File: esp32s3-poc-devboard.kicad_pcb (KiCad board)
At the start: 4 copper layers, 74 x 66.8 mm, 104 parts, among them J1 24VDC, J2 Conn_01x01_Pin, J3 USB_C_Receptacle_USB2.0_14P, J4 USB_C_Receptacle_USB2.0_14P, J5 Screw_Terminal_01x06, J6 Conn_Coaxial, J7 Conn_01x16_Pin, J8 Screw_Terminal_01x04, Q3 MMDT5551, SW1 SW_Push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

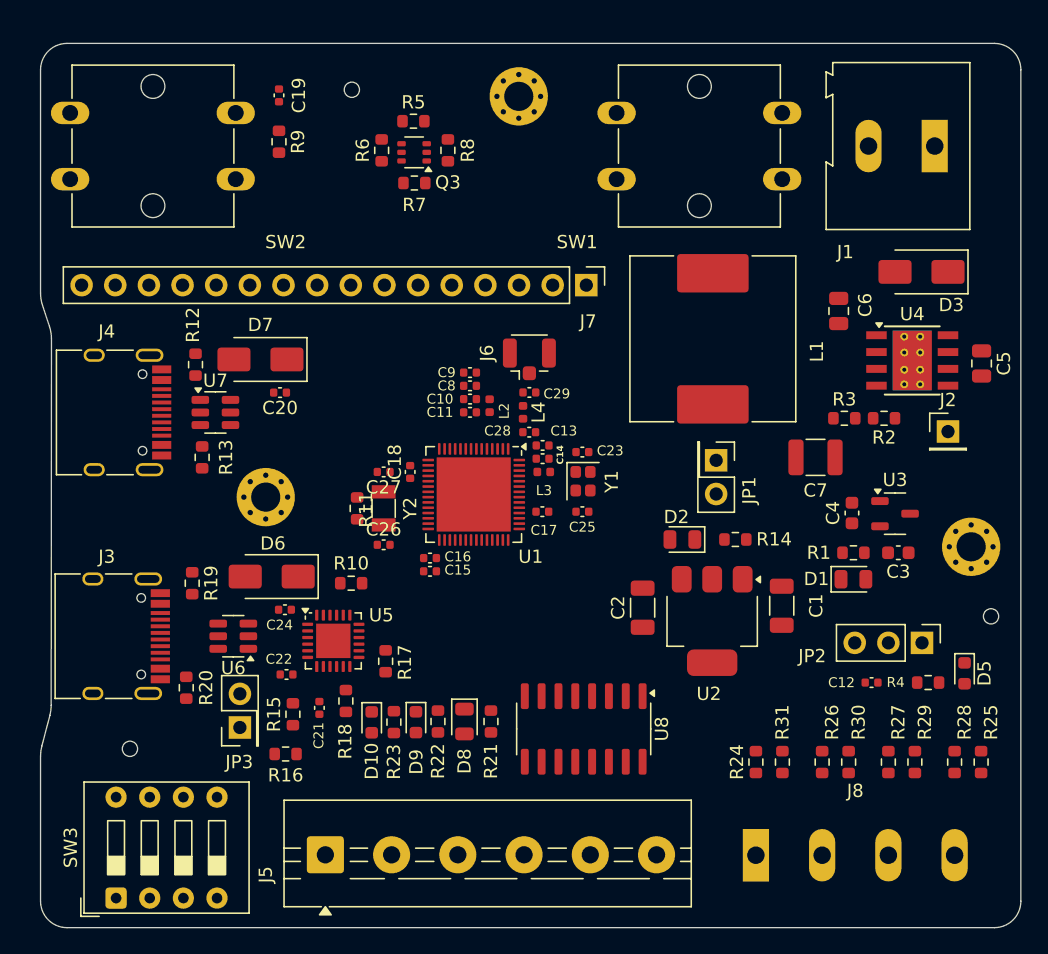
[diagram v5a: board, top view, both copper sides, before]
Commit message: add fiducials
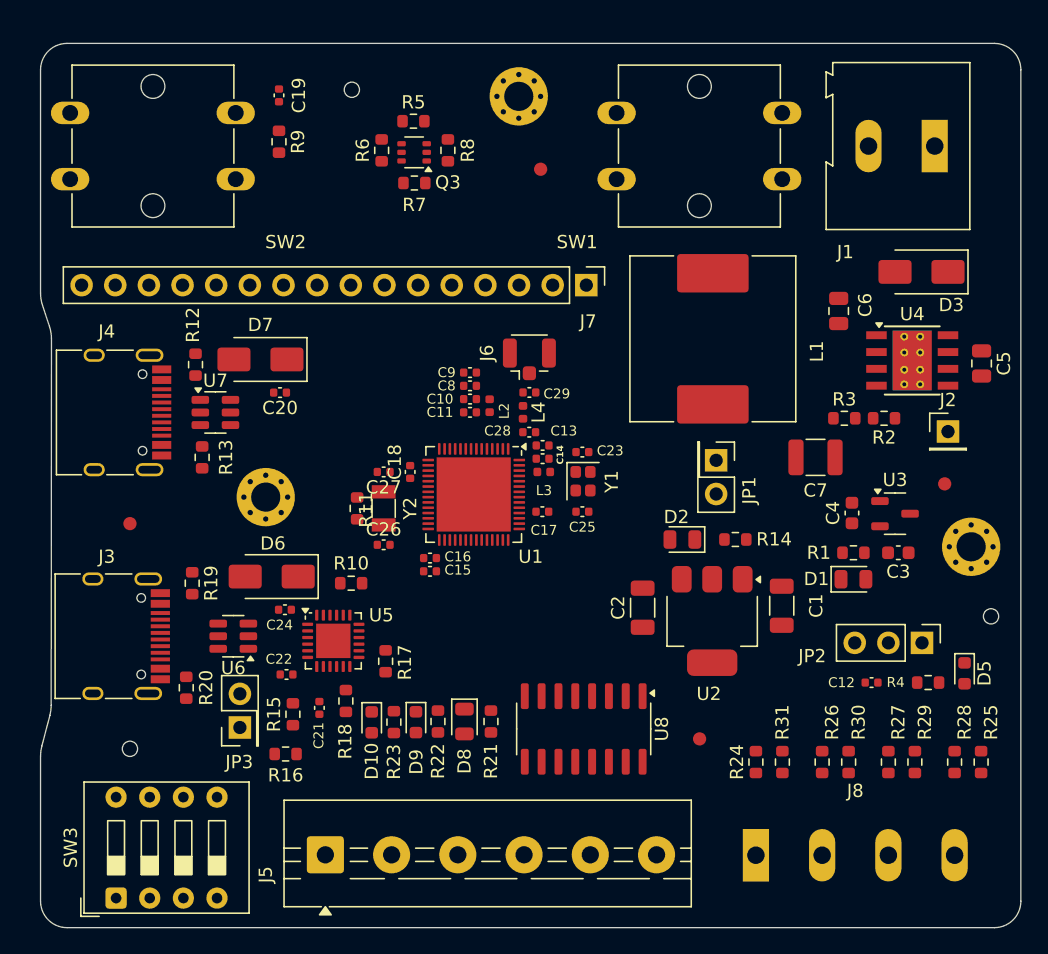
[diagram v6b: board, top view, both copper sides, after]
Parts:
- added ?: , , F.Cu at (172.2, 103.2)
- added ?: , , F.Cu at (190.8, 84.0)
- added ?: , , F.Cu at (160.2, 60.2)
- added REF**: Fiducial_1mm_Mask2mm, Fiducial:Fiducial_1mm_Mask2mm, F.Cu at (129.2, 87.0)

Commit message: add ground vias
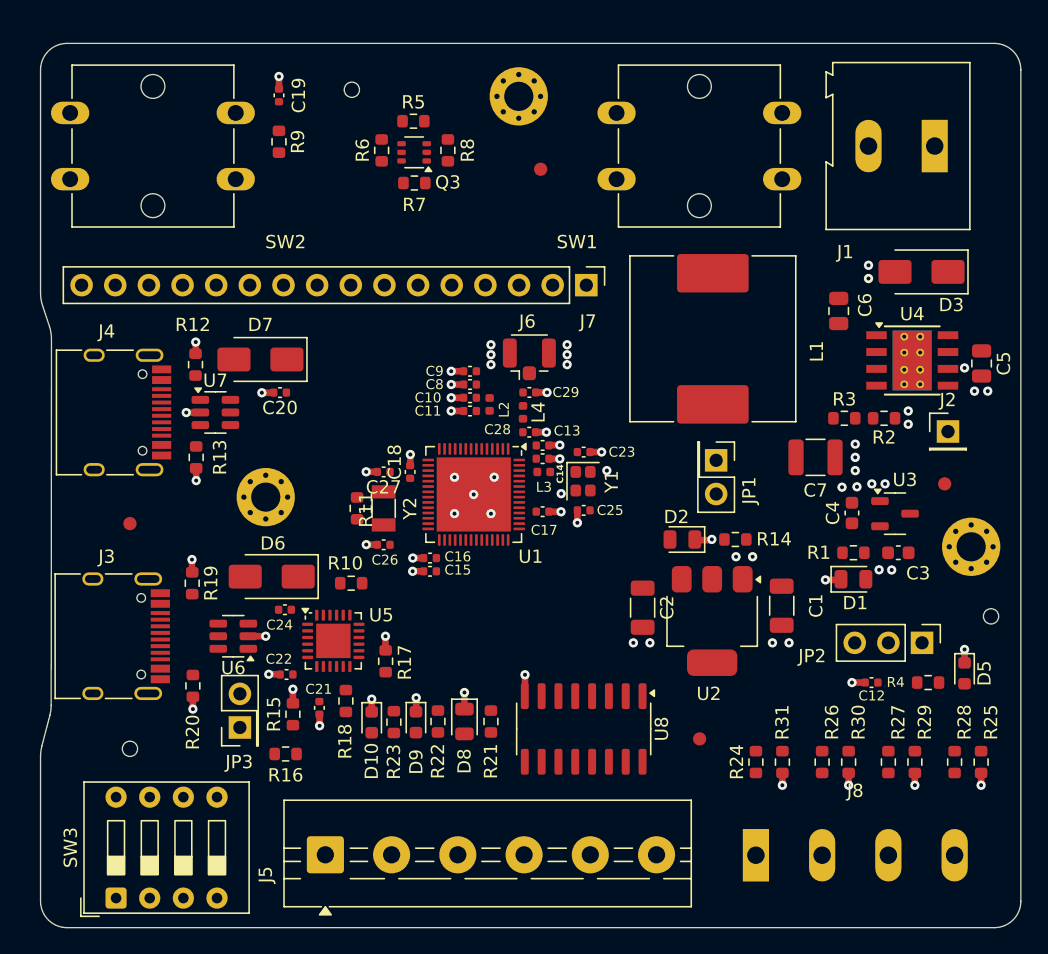
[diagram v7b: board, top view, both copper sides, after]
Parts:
- moved R20 0.52 mm to (134.0, 99.2)
- moved R13 0.45 mm to (134.2, 82.0)
- moved C25 0.14 mm to (163.5, 86.0)
- moved C10 0.10 mm to (154.9, 77.5)
- moved C11 0.10 mm to (154.9, 78.5)
- moved C23 0.10 mm to (163.5, 81.6)
- moved C8 0.10 mm to (154.9, 76.5)
- moved C9 0.10 mm to (154.9, 75.5)
- moved L2 0.10 mm to (156.4, 78.0)
- turned C2 to -90 degrees
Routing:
- net GND: track 0.00 -> 33.0 mm, vias 0 -> 75

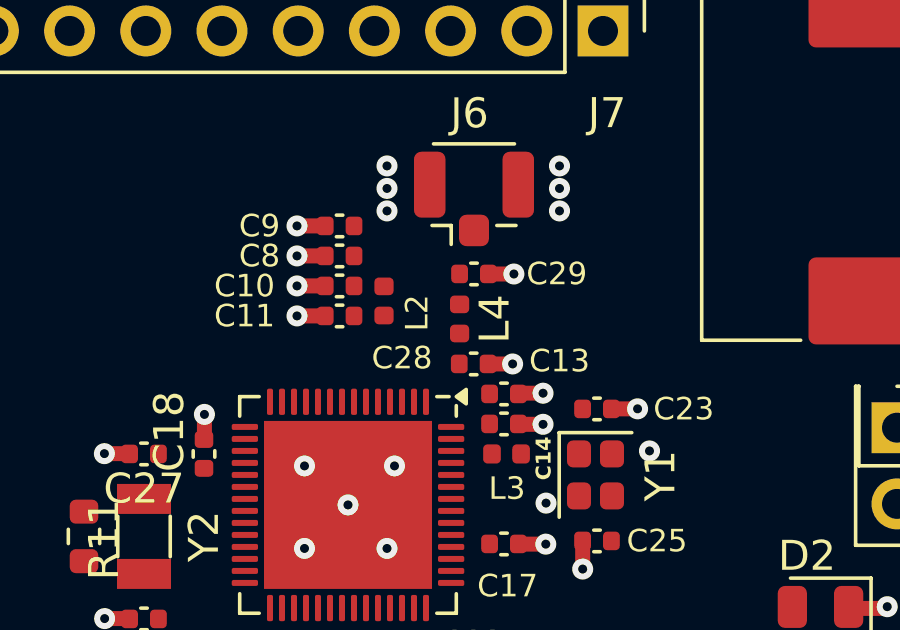
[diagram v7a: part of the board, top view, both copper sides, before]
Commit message: add rf routing
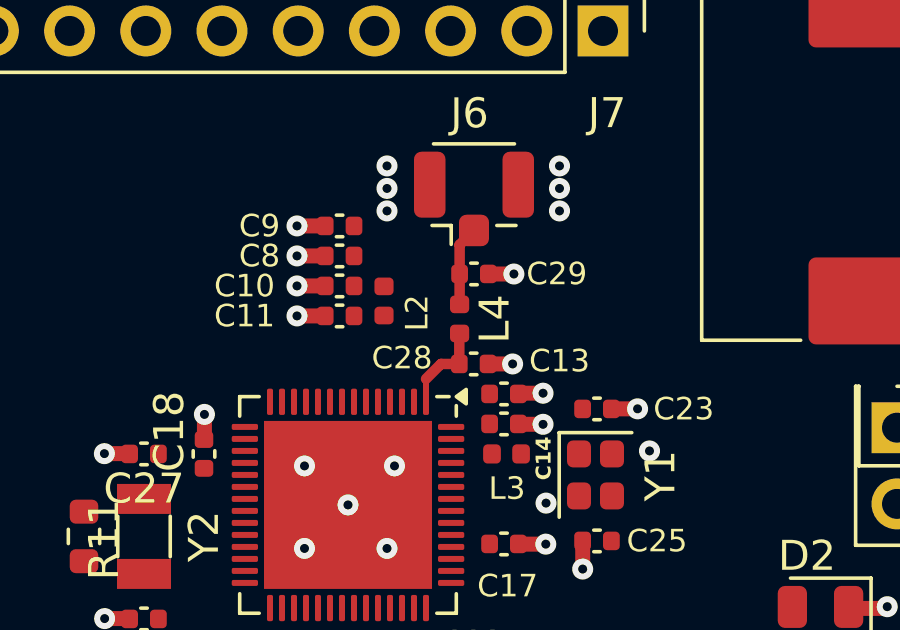
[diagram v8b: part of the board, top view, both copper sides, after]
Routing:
- net /RF: track 0.00 -> 3.10 mm
- net /RF_ANT: track 0.00 -> 2.66 mm
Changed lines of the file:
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@@
 		(net 1)
+	)
+	(segment
+		(start 158.3 80.1)
+		(end 158.91 80.1)
+		(width 0.3493)
+		(layer "F.Cu")
+		(net 18)
+	)
+	(segment
+		(start 157.8 80.8)
+		(end 157.8 80.6)
+		(width 0.2)
+		(layer "F.Cu")
+		(net 18)
+	)
+	(segment
+		(start 158.91 79.095)
+		(end 158.92 79.085)
+		(width 0.3493)
+		(layer "F.Cu")
+		(net 18)
+	)
+	(segment
+		(start 158.91 80.1)
+		(end 158.91 79.095)
+		(width 0.3493)
+		(layer "F.Cu")
+		(net 18)
+	)
+	(segment
+		(start 157.8 80.6)
+		(end 158.3 80.1)
+		(width 0.3493)
+		(layer "F.Cu")
+		(net 18)
+	)
+	(segment
+		(start 157.8 81.3625)
+		(end 157.8 80.8)
+		(width 0.2)
+		(layer "F.Cu")
+		(net 18)
+	)
+	(segment
+		(start 158.92 78.115)
+		(end 158.92 77.1)
+		(width 0.3493)
+		(layer "F.Cu")
+		(net 19)
+	)
+	(segment
+		(start 158.92 76.13)
+		(end 159.4 75.65)
+		(width 0.3493)
+		(layer "F.Cu")
+		(net 19)
+	)
+	(segment
+		(start 158.92 77.1)
+		(end 158.92 76.13)
+		(width 0.3493)
+		(layer "F.Cu")
+		(net 19)
+	)
+	(zone
+		(net 18)
+		(net_name "/RF")
+		(layer "F.Cu")
+		(name "$teardrop_track$")
+		(hatch none 0.1)
+		(priority 30000)
+		(attr
+			(teardrop
+				(type track_end)
+			)
+		)
+		(connect_pads yes
+			(clearance 0)
+		)
+		(min_thickness 0.0254)
+		(filled_areas_thickness no)
+		(fill yes
+			(thermal_gap 0.5)
+			(thermal_bridge_width 0.5)
+			(island_removal_mode 1)
+			(island_area_min 10)
+		)
+		(polygon
+			(pts
+				(xy 157.7 80.945944) (xy 157.9 80.945944) (xy 157.971294 80.634073) (xy 157.8 80.599) (xy 157.628706 80.634073)
+			)
+		)
 	)
 	(zone
